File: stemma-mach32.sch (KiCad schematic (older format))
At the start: 28 parts, among them J1 Conn_01x09_Male, J2 Conn_01x04_Male, J3 Conn_01x04_Male, J4 Conn_01x09_Male, J5 DebugEdge_02x04, Q1 BSS138, Q2 BSS138, U1 AP2112K-3.3, U2 MACHXO2-32QFN

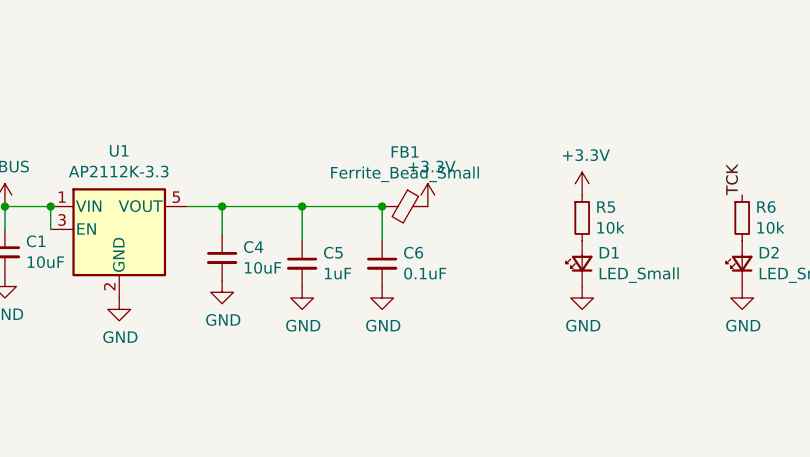
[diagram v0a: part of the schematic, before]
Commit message: Added suggested part numbers to the BOM
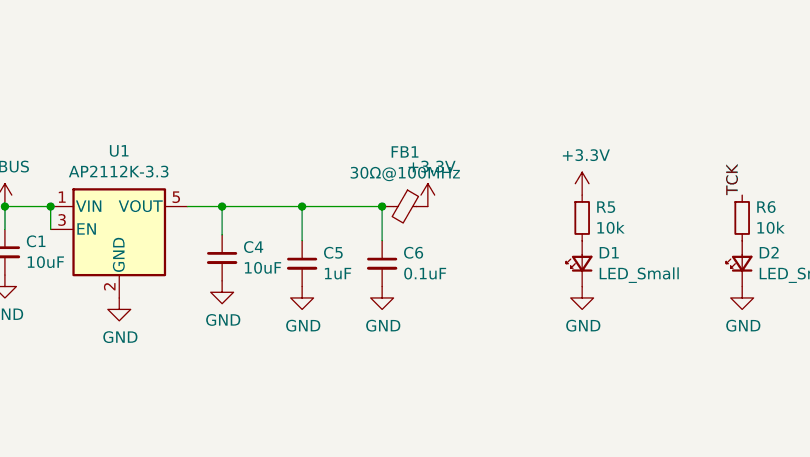
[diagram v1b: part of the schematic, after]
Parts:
- C1, C4: LCSC Part # (none) -> C19702; Part # (none) -> CL10A106KP8NNNC
- C10, C2, C3, C6, C7, C8, C9: LCSC Part # (none) -> C15725; Part # (none) -> CL10B104KC8NNNC
- C5: LCSC Part # (none) -> C15849; Part # (none) -> CL10A105KB8NNNC
- D1, D2: LCSC Part # (none) -> C85323; Part # (none) -> NCD0603A1
- FB1: value Ferrite_Bead_Small -> 30Ω@100MHz; LCSC Part # (none) -> C17305; Part # (none) -> BLM18PG300SN1D
- Q1, Q2: LCSC Part # (none) -> C426569; Part # (none) -> C426569
- R1, R2, R3, R4: LCSC Part # (none) -> C23162; Part # (none) -> 0603WAF4701T5E
- R5, R6: LCSC Part # (none) -> C25804; Part # (none) -> 0603WAF1002T5E
- U1: LCSC Part # (none) -> C51118; Part # (none) -> AP2112K-3.3TRG1
- U2: Part # (none) -> LCMXO2-1200HC-4MG132I
